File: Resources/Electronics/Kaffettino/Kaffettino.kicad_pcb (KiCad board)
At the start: 2 copper layers, 43 parts, among them J1 PPTC101LFBN-RC, J2 OSTVN02A150, M1 RFID-RC522, U1 PCF8574AN, U2 ESP32-38Pin-Wroom, U3 DFR0299

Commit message: Corrected some footprints in the PCB schema
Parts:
- added H1: MountingHole, MountingHole:MountingHole_3.2mm_M3, F.Cu at (183.0, 128.0)
- added H2: MountingHole, MountingHole:MountingHole_3.2mm_M3, F.Cu at (183.0, 38.0)
- added H3: MountingHole, MountingHole:MountingHole_3.2mm_M3, F.Cu at (93.0, 38.0)
- added H4: MountingHole, MountingHole:MountingHole_3.2mm_M3, F.Cu at (93.0, 128.0)
- added J3: OSTVN04A150, OSTVN04A150:CONN_OSTVN04A150_OST, F.Cu at (173.2, 127.4)
- added J5: OSTVN04A150, OSTVN04A150:CONN_OSTVN04A150_OST, F.Cu at (173.2, 119.2)
- added R12: 1k, Resistor_THT:R_Axial_DIN0207_L6.3mm_D2.5mm_P10.16mm_Horizontal, F.Cu at (109.0, 109.2)
- added R23: 1k, Resistor_THT:R_Axial_DIN0207_L6.3mm_D2.5mm_P10.16mm_Horizontal, F.Cu at (109.0, 112.9)
- added R24: 10k, Resistor_THT:R_Axial_DIN0207_L6.3mm_D2.5mm_P10.16mm_Horizontal, F.Cu at (109.0, 116.5)
- R25: value 1k -> 10k
- moved J1 127.5 mm to (151.3, 36.1), turned to 0 degrees
- moved Brd1 125.3 mm to (125.3, 36.1), turned to 180 degrees
- moved R8 97.1 mm to (174.2, 65.1)
- moved C1 95.4 mm to (176.8, 99.5), turned to 0 degrees
- moved R4 92.0 mm to (174.2, 52.2)
- moved R9 90.9 mm to (170.9, 65.1)
- moved R25 87.8 mm to (126.6, 67.3), turned to 0 degrees
- moved C2 87.8 mm to (174.3, 96.4), turned to 0 degrees
- moved R5 85.8 mm to (170.9, 52.2)
- moved R19 84.7 mm to (167.7, 65.1)
- moved C6 82.5 mm to (171.8, 99.5), turned to 180 degrees
- moved R15 79.6 mm to (167.7, 52.2)
- moved R20 78.5 mm to (164.4, 65.1)
- moved C7 74.9 mm to (169.2, 96.4), turned to 180 degrees
- moved R16 73.3 mm to (164.4, 52.2)
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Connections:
- J2 pad 1: GNDREF -> +5V
- J2 pad 2: +5V -> GNDREF
- M1 pad 5: unconnected-(M1-IRQ-Pad5) -> /RFID_INT
- R25 pad 2: Net-(U1-*INT) -> /KP_INT
- U1 pad 13: Net-(U1-*INT) -> /KP_INT
- U2 pad 10: /GREEN -> /YELLOW
- U2 pad 11: unconnected-(U2-GPIO25-Pad11) -> /GREEN
- U2 pad 14: unconnected-(U2-GPIO35-Pad14) -> /EXPANSION_1
- U2 pad 16: unconnected-(U2-GPIO39-Pad16) -> /RFID_INT
- U2 pad 17: unconnected-(U2-GPIO36-Pad17) -> /KP_INT
- U2 pad 28: unconnected-(U2-GPIO17-Pad28) -> /EXPANSION_2
- U2 pad 8: /RED -> unconnected-(U2-GPIO14-Pad8)
- U2 pad 9: /YELLOW -> /RED
- U3 pad 2: /MICRO_SD_RX -> Net-(U3-RX)
- U3 pad 3: /MICRO_SD_TX -> Net-(U3-TX)
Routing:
- net GNDREF: track 276.2 -> 0.00 mm
- net +3.3V: track 125.8 -> 0.00 mm
- net Net-(J1-Pad2): track 95.5 -> 0.00 mm
- net Net-(J1-Pad3): track 86.9 -> 0.00 mm
- net Net-(J1-Pad4): track 78.4 -> 0.00 mm
- net /RED: track 77.7 -> 0.00 mm
- net /YELLOW: track 75.6 -> 0.00 mm
- net /GREEN: track 73.6 -> 0.00 mm
- net Net-(J1-Pad5): track 69.8 -> 0.00 mm
- net Net-(J1-Pad6): track 46.1 -> 0.00 mm
- net /KP_C1: track 47.6 -> 7.78 mm
- net /KP_C2: track 39.5 -> 3.80 mm
- net Net-(J1-Pad7): track 35.5 -> 0.00 mm
- net Net-(J1-Pad8): track 25.0 -> 0.00 mm
- net /KP_C3: track 31.3 -> 7.81 mm
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- added copper zone on B.Cu, net GNDREF
- added copper zone on F.Cu, net GNDREF
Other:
- board outline added: 100 x 100 mm

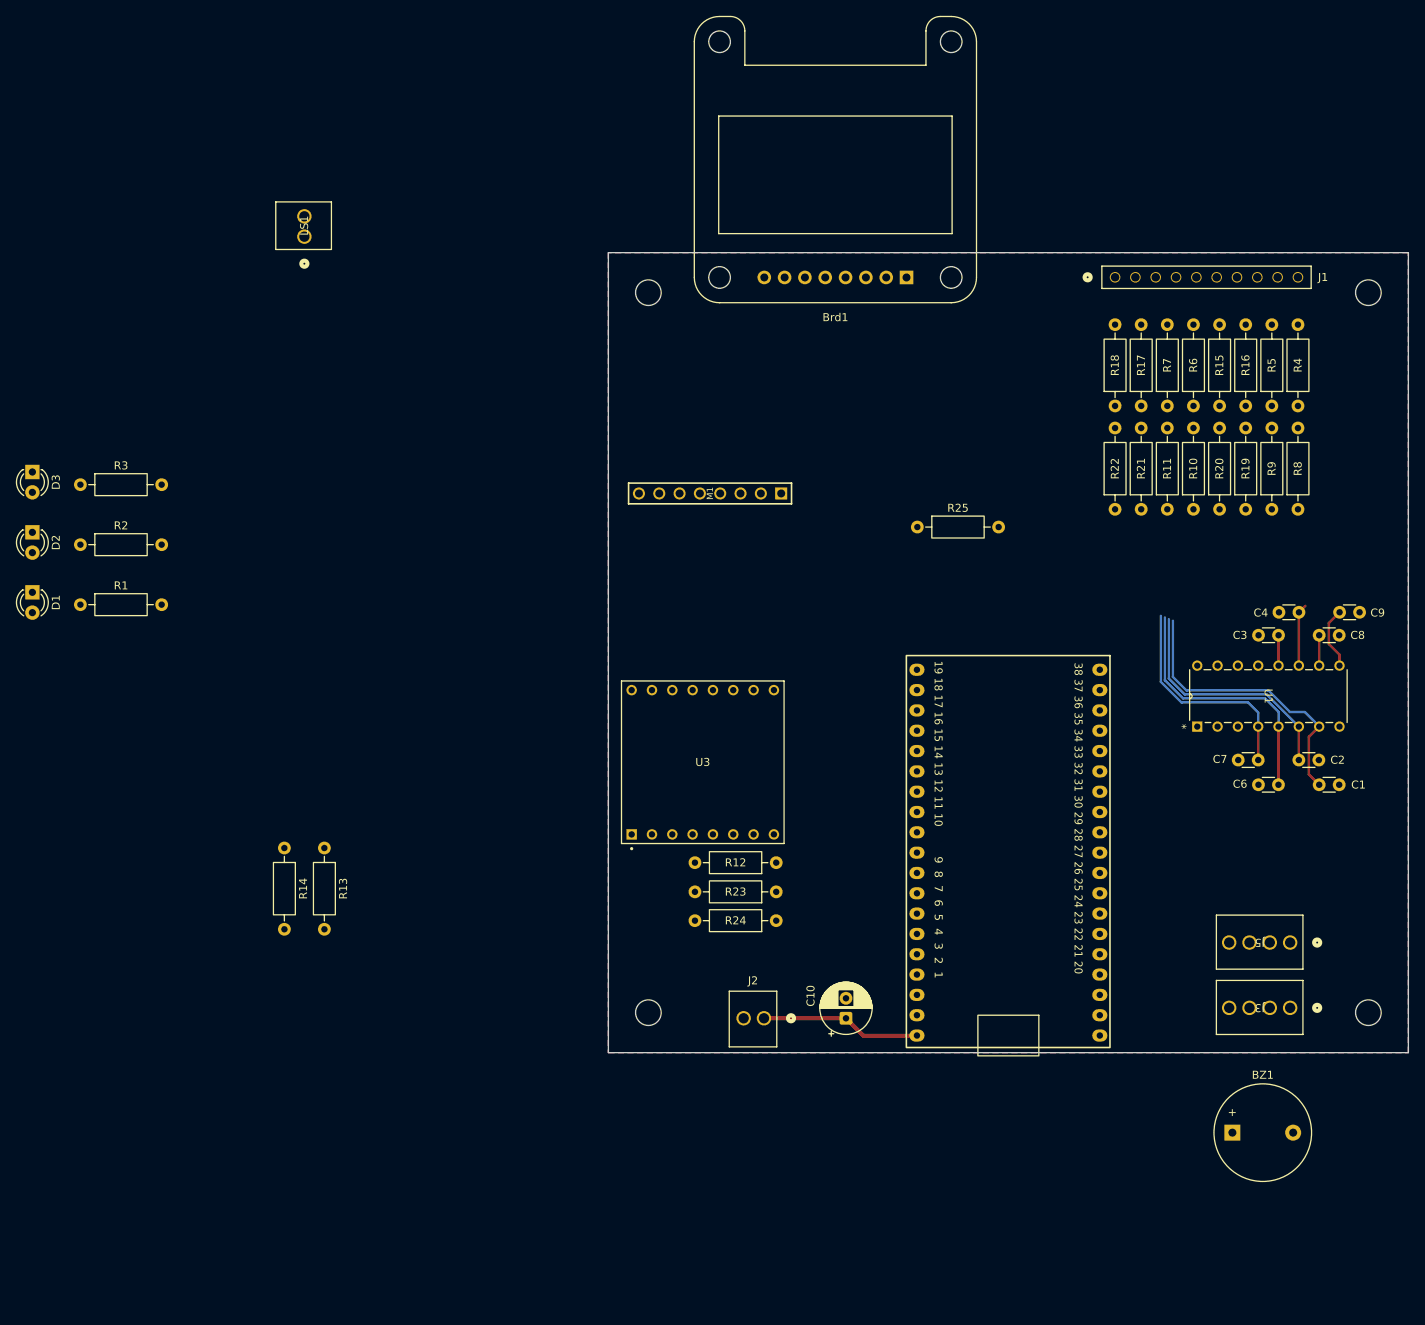
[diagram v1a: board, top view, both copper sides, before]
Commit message: Trying images on display and almost finished PCB design.
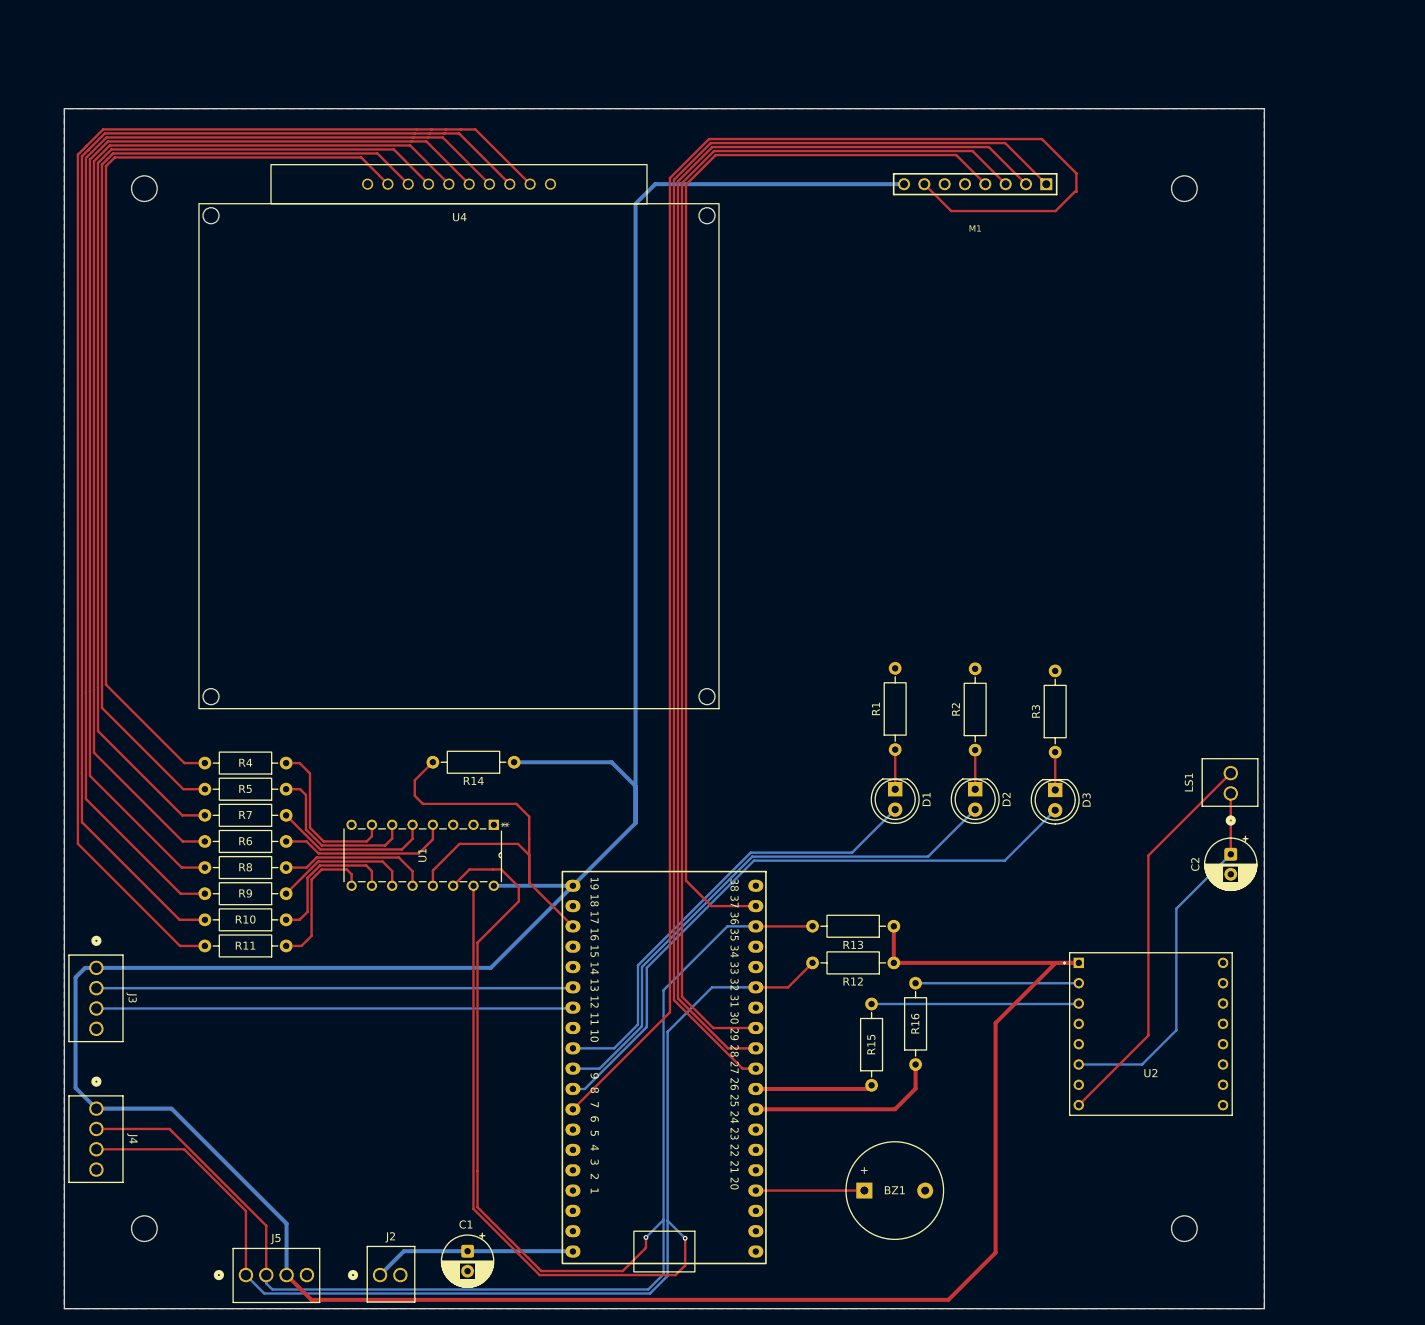
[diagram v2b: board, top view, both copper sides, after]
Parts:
- removed Brd1: SSD1306, Display:Adafruit_SSD1306
- removed C10: 4.7uF, Capacitor_THT:CP_Radial_D6.3mm_P2.50mm
- removed C3, C4, C6, C7, C8, C9: 100nF, Capacitor_THT:C_Disc_D3.0mm_W1.6mm_P2.50mm
- removed J1: PPTC101LFBN-RC, PPTC101LFBN_RC:CONN10_101LFBN-RC_SUL
- removed R17, R18, R23: 1k, Resistor_THT:R_Axial_DIN0207_L6.3mm_D2.5mm_P10.16mm_Horizontal
- removed R19, R20, R21, R22, R24, R25: 10k, Resistor_THT:R_Axial_DIN0207_L6.3mm_D2.5mm_P10.16mm_Horizontal
- added J4: OSTVN04A150, OSTVN04A150:CONN_OSTVN04A150_OST, F.Cu at (24.0, 140.0)
- added U4: 26052, 26052 matrix keypad 4x4:26052 matrix keypad 4x4, F.Cu at (101.8, 22.0)
- C1, C2: value 100nF -> 4.7uF; footprint Capacitor_THT:C_Disc_D3.0mm_W1.6mm_P2.50mm -> Capacitor_THT:CP_Radial_D6.3mm_P2.50mm
- D1, D2, D3: footprint LED_THT:LED_D3.0mm -> LED_THT:LED_D5.0mm
- R10, R11, R8, R9: value 10k -> 1k
- R14: value 1k -> 10k
- U2: value ESP32-38Pin-Wroom -> DFR0299; footprint ESP32-38Pin:ESP32_38pin -> DFR0299:MODULE_DFR0299
- U3: value DFR0299 -> ESP32-38Pin-Wroom; footprint DFR0299:MODULE_DFR0299 -> ESP32-38Pin:ESP32_38pin
- moved J3 149.3 mm to (24.0, 122.4), turned to -90 degrees
- moved J5 137.0 mm to (42.7, 160.8), turned to 0 degrees
- moved LS1 135.1 mm to (165.8, 100.6)
- moved R8 134.2 mm to (47.7, 109.9), turned to 180 degrees
- moved R4 134.1 mm to (47.7, 96.8), turned to 180 degrees
- moved D3 133.9 mm to (143.8, 100.2)
- moved R9 132.2 mm to (47.7, 113.1), turned to 180 degrees
- moved R5 132.2 mm to (47.7, 100.1), turned to 180 degrees
- moved U1 126.5 mm to (55.9, 112.1), turned to -90 degrees
- moved R3 126.4 mm to (143.8, 95.4), turned to 90 degrees
- moved R10 124.5 mm to (47.7, 116.4), turned to 180 degrees
- moved R6 124.4 mm to (47.7, 103.3), turned to 180 degrees
- moved R11 122.9 mm to (47.7, 119.7), turned to 180 degrees
- moved R7 122.9 mm to (47.7, 106.6), turned to 180 degrees
- moved D2 122.1 mm to (133.8, 100.1)
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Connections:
- C1 pad 1: /KP_R4 -> +5V
- C2 pad 1: /KP_R3 -> Net-(U2-SPK1)
- J5 pad 1: +3.3V -> /GEN_SDA
- J5 pad 3: /GEN_SDA -> +3.3V
- LS1 pad 1: Net-(U3-SPK1) -> Net-(U2-SPK1)
- LS1 pad 2: Net-(U3-SPK2) -> Net-(U2-SPK2)
- M1 pad 5: /RFID_INT -> unconnected-(M1-IRQ-Pad5)
- R10 pad 1: +3.3V -> /KP_C2
- R10 pad 2: /KP_C4 -> Net-(U4-C2)
- R11 pad 1: +3.3V -> /KP_C1
- R11 pad 2: /KP_C3 -> Net-(U4-C1)
- R12 pad 1: /MICRO_SD_TX -> +3.3V
- R12 pad 2: Net-(U3-TX) -> /GEN_SDA
- R13 pad 2: /GEN_SDA -> /GEN_SCL
- R14 pad 2: /GEN_SCL -> /KP_INT
- R15 pad 1: /KP_R2 -> /MICRO_SD_TX
- R15 pad 2: Net-(J1-Pad7) -> Net-(U2-TX)
- R16 pad 1: /KP_R1 -> /MICRO_SD_RX
- R16 pad 2: Net-(J1-Pad6) -> Net-(U2-RX)
- R6 pad 1: /KP_C4 -> /KP_R2
- R7 pad 1: /KP_C3 -> /KP_R1
- R8 pad 1: +3.3V -> /KP_C4
- R8 pad 2: /KP_R4 -> Net-(U4-C4)
- R9 pad 1: +3.3V -> /KP_C3
- R9 pad 2: /KP_R3 -> Net-(U4-C3)
- U2 pad 1: +5V -> +3.3V
- U2 pad 10: /YELLOW -> GNDREF
- U2 pad 11: /GREEN -> unconnected-(U2-IO2-Pad11)
- U2 pad 12: /MICRO_SD_RX -> unconnected-(U2-ADKEY1-Pad12)
- U2 pad 13: /MICRO_SD_TX -> unconnected-(U2-ADKEY2-Pad13)
- U2 pad 14: /EXPANSION_1 -> unconnected-(U2-USB+-Pad14)
- U2 pad 15: /RFID_RST -> unconnected-(U2-USB--Pad15)
- U2 pad 16: /RFID_INT -> unconnected-(U2-BUSY-Pad16)
- U2 pad 2: unconnected-(U2-GPIO11-Pad2) -> Net-(U2-RX)
- U2 pad 3: unconnected-(U2-GPIO10-Pad3) -> Net-(U2-TX)
- U2 pad 6: GNDREF -> Net-(U2-SPK1)
- U2 pad 7: unconnected-(U2-GPIO12-Pad7) -> GNDREF
- U2 pad 8: unconnected-(U2-GPIO14-Pad8) -> Net-(U2-SPK2)
- U2 pad 9: /RED -> unconnected-(U2-IO1-Pad9)
- U3 pad 1: +3.3V -> +5V
- U3 pad 10: GNDREF -> /YELLOW
- U3 pad 11: unconnected-(U3-IO2-Pad11) -> /GREEN
- U3 pad 13: unconnected-(U3-ADKEY2-Pad13) -> /EXPANSION_2
- U3 pad 14: unconnected-(U3-USB+-Pad14) -> /EXPANSION_1
- U3 pad 2: Net-(U3-RX) -> unconnected-(U3-GPIO11-Pad2)
- U3 pad 3: Net-(U3-TX) -> unconnected-(U3-GPIO10-Pad3)
- U3 pad 6: Net-(U3-SPK1) -> GNDREF
- U3 pad 7: GNDREF -> unconnected-(U3-GPIO12-Pad7)
- U3 pad 8: Net-(U3-SPK2) -> /RFID_RST
- U3 pad 9: unconnected-(U3-IO1-Pad9) -> /RED
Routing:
- net +3.3V: track 0.00 -> 436.8 mm
- net /GEN_SCL: track 0.00 -> 223.7 mm, vias 0 -> 1
- net /GEN_SDA: track 0.00 -> 213.9 mm, vias 0 -> 1
- net /RFID_RST: track 0.00 -> 199.7 mm
- net Net-(U4-C1): track 0.00 -> 168.0 mm
- net /RFID_SDA: track 0.00 -> 166.9 mm
- net /RFID_SCK: track 0.00 -> 161.6 mm
- net Net-(U4-C2): track 0.00 -> 161.0 mm
- net /RFID_MOSI: track 0.00 -> 156.4 mm
- net Net-(U4-C3): track 0.00 -> 153.8 mm
- net Net-(U4-C4): track 0.00 -> 146.7 mm
- net Net-(U4-R1): track 0.00 -> 139.6 mm
- net /RFID_MISO: track 0.00 -> 137.5 mm
- net Net-(U4-R2): track 0.00 -> 132.6 mm
- net Net-(U4-R3): track 0.00 -> 125.4 mm
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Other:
- board size 100 x 100 mm -> 150 x 150 mm

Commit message: Finished routing in PCB, waiting for approval
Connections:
- U3 pad 31: /RFID_MOSI -> /RFID_MISO
- U3 pad 37: /RFID_MISO -> /RFID_MOSI
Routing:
- net GNDREF: track 0.00 -> 22.0 mm, vias 0 -> 5
- net /RFID_MOSI: track 156.4 -> 141.1 mm, vias 0 -> 1
- net /RFID_MISO: track 137.5 -> 150.7 mm
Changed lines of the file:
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@@
 			(layers "*.Cu" "*.Mask")
 			(remove_unused_layers no)
-			(net 19 "/RFID_MOSI")
+			(net 20 "/RFID_MISO")
 			(pinfunction "GPIO19")
 			(pintype "bidirectional")
@@
 			(layers "*.Cu" "*.Mask")
 			(remove_unused_layers no)
-			(net 20 "/RFID_MISO")
+			(net 19 "/RFID_MOSI")
 			(pinfunction "GPIO23")
 			(pintype "bidirectional")
@@
 	)
 	(segment
-		(start 35.002806 96.802857)
-		(end 25.202 87.002051)
+		(start 25.2 87.000052)
+		(end 35.002806 96.802857)
 		(width 0.3)
 		(layer "F.Cu")
@@
 	)
 	(segment
-		(start 25.202 87.002051)
-		(end 25.2 87.000052)
-		(width 0.3)
-		(layer "F.Cu")
-		(net 3)
-	)
-	(segment
 		(start 52.161468 110.107)
 		(end 50.901 111.367468)
@@
 	)
 	(segment
-		(start 101.20852 20.3)
-		(end 133.52 20.3)
+		(start 101.41504 20.802)
+		(end 114.602 20.802)
 		(width 0.3)
 		(layer "F.Cu")
@@
 	)
 	(segment
-		(start 106.43 129.92)
-		(end 101.12 129.92)
+		(start 97.701 24.51604)
+		(end 101.41504 20.802)
 		(width 0.3)
 		(layer "F.Cu")
@@
 	)
 	(segment
+		(start 114.602 20.802)
+		(end 121.4 27.6)
+		(width 0.3)
+		(layer "F.Cu")
+		(net 19)
+	)
+	(segment
+		(start 97.701 105.951)
+		(end 97.701 37.6)
+		(width 0.3)
+		(layer "F.Cu")
+		(net 19)
+	)
+	(segment
+		(start 97.701 37.6)
+		(end 97.701 24.51604)
+		(width 0.3)
+		(layer "F.Cu")
+		(net 19)
+	)
+	(segment
+		(start 106.43 114.68)
+		(end 97.701 105.951)
+		(width 0.3)
+		(layer "F.Cu")
+		(net 19)
+	)
+	(via
+		(at 121.4 27.6)
+		(size 0.6)
+		(drill 0.3)
+		(layers "F.Cu" "B.Cu")
+		(net 19)
+	)
+	(segment
+		(start 121.4 27.6)
+		(end 123.5 29.7)
+		(width 0.3)
+		(layer "B.Cu")
+		(net 19)
+	)
+	(segment
+		(start 123.5 29.7)
+		(end 132.4 29.7)
+		(width 0.3)
+		(layer "B.Cu")
+		(net 19)
+	)
+	(segment
+		(start 132.4 29.7)
+		(end 137.66 24.44)
+		(width 0.3)
+		(layer "B.Cu")
+		(net 19)
+	)
+	(segment
+		(start 135.12 24.44)
+		(end 130.981 20.301)
+		(width 0.3)
+		(layer "F.Cu")
+		(net 20)
+	)
+	(segment
+		(start 101.20752 20.301)
+		(end 97.2 24.30852)
+		(width 0.3)
+		(layer "F.Cu")
+		(net 20)
+	)
+	(segment
+		(start 97.2 120.69)
+		(end 106.43 129.92)
+		(width 0.3)
+		(layer "F.Cu")
+		(net 20)
+	)
+	(segment
+		(start 130.981 20.301)
+		(end 101.20752 20.301)
+		(width 0.3)
+		(layer "F.Cu")
+		(net 20)
+	)
+	(segment
 		(start 97.2 24.30852)
-		(end 101.20852 20.3)
-		(width 0.3)
-		(layer "F.Cu")
-		(net 19)
-	)
-	(segment
-		(start 101.12 129.92)
-		(end 97.2 126)
-		(width 0.3)
-		(layer "F.Cu")
-		(net 19)
-	)
-	(segment
-		(start 97.2 126)
-		(end 97.2 24.30852)
-		(width 0.3)
-		(layer "F.Cu")
-		(net 19)
-	)
-	(segment
-		(start 133.52 20.3)
-		(end 137.66 24.44)
-		(width 0.3)
-		(layer "F.Cu")
-		(net 19)
-	)
-	(segment
-		(start 100.881 114.68)
-		(end 97.701 111.5)
+		(end 97.2 120.69)
 		(width 0.3)
 		(layer "F.Cu")
 		(net 20)
 	)
-	(segment
-		(start 97.701 111.5)
-		(end 97.701 24.51604)
-		(width 0.3)
-		(layer "F.Cu")
-		(net 20)
-	)
-	(segment
-		(start 106.43 114.68)
-		(end 100.881 114.68)
-		(width 0.3)
-		(layer "F.Cu")
-		(net 20)
-	)
-	(segment
-		(start 101.41704 20.8)
-		(end 131.48 20.8)
-		(width 0.3)
-		(layer "F.Cu")
-		(net 20)
-	)
-	(segment
-		(start 97.701 24.51604)
-		(end 101.41704 20.8)
-		(width 0.3)
-		(layer "F.Cu")
-		(net 20)
-	)
-	(segment
-		(start 131.48 20.8)
-		(end 135.12 24.44)
-		(width 0.3)
-		(layer "F.Cu")
-		(net 20)
+	(via
+		(at 144.2 151.6)
+		(size 0.6)
+		(drill 0.3)
+		(layers "F.Cu" "B.Cu")
+		(free yes)
+		(net 22)
+	)
+	(via
+		(at 40.8 134.3)
+		(size 0.6)
+		(drill 0.3)
+		(layers "F.Cu" "B.Cu")
+		(free yes)
+		(net 22)
+	)
+	(via
+		(at 107.8 31.2)
+		(size 0.6)
+		(drill 0.3)
+		(layers "F.Cu" "B.Cu")
+		(free yes)
+		(net 22)
+	)
+	(via
+		(at 158.3 90.7)
+		(size 0.6)
+		(drill 0.3)
+		(layers "F.Cu" "B.Cu")
+		(free yes)
+		(net 22)
+	)
+	(via
+		(at 65.4 59.3)
+		(size 0.6)
+		(drill 0.3)
+		(layers "F.Cu" "B.Cu")
+		(free yes)
+		(net 22)
+	)
+	(segment
+		(start 109.62 127.38)
+		(end 110.6 126.4)
+		(width 0.2)
+		(layer "B.Cu")
+		(net 22)
+	)
+	(segment
+		(start 110.6 126.4)
+		(end 110.6 113.9)
+		(width 0.2)
+		(layer "B.Cu")
+		(net 22)
+	)
+	(segment
+		(start 110.6 113.9)
+		(end 108.84 112.14)
+		(width 0.2)
+		(layer "B.Cu")
+		(net 22)
+	)
+	(segment
+		(start 108.84 112.14)
+		(end 106.43 112.14)
+		(width 0.2)
+		(layer "B.Cu")
+		(net 22)
+	)
+	(segment
+		(start 106.43 127.38)
+		(end 109.62 127.38)
+		(width 0.2)
+		(layer "B.Cu")
+		(net 22)
 	)
 	(segment
@@
 	(segment
 		(start 71.641 119.259)
-		(end 71.641 147.8)
+		(end 71.641 152.33248)
 		(width 0.3)
 		(layer "F.Cu")
@@
 	(segment
 		(start 70.64 110.1)
-		(end 73.6 110.1)
+		(end 74.6 110.1)
 		(width 0.3)
 		(layer "F.Cu")
@@
 	)
 	(segment
-		(start 73.6 110.1)
-		(end 74.6 110.1)
-		(width 0.3)
-		(layer "F.Cu")
-		(net 26)
-	)
-	(segment
-		(start 71.641 147.8)
-		(end 71.641 152.33248)
-		(width 0.3)
-		(layer "F.Cu")
-		(net 26)
-	)
-	(segment
-		(start 92.6 157.5)
-		(end 92.7 157.4)
-		(width 0.3)
-		(layer "F.Cu")
-		(net 26)
-	)
-	(segment
-		(start 73.2 117.7)
-		(end 71.641 119.259)
+		(start 71.641 119.259)
+		(end 76.8 114.1)
 		(width 0.3)
 		(layer "F.Cu")
@@
 	(segment
 		(start 89.8 160.3)
-		(end 92.6 157.5)
+		(end 92.7 157.4)
 		(width 0.3)
 		(layer "F.Cu")
@@
 	)
 	(segment
-		(start 79.25426 159.94574)
+		(start 71.641 152.33248)
 		(end 79.60852 160.3)
-		(width 0.3)
-		(layer "F.Cu")
-		(net 26)
-	)
-	(segment
-		(start 76.8 114.1)
-		(end 73.2 117.7)
-		(width 0.3)
-		(layer "F.Cu")
-		(net 26)
-	)
-	(segment
-		(start 71.641 152.33248)
-		(end 79.25426 159.94574)
 		(width 0.3)
 		(layer "F.Cu")
@@
 	(segment
 		(start 78.1 111.75)
-		(end 78.1 106.3)
+		(end 78.1 103.5)
 		(width 0.3)
 		(layer "F.Cu")
@@
 		(width 0.3)
 		(layer "F.Cu")
-		(net 30)
-	)
-	(segment
-		(start 78.1 103.5)
-		(end 78.1 106.3)
-		(width 0.3)
-		(layer "F.Cu")
